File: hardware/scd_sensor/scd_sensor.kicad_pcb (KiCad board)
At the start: 2 copper layers, 18.6 x 27.4 mm, 10 parts, among them J1 Conn_01x03, J5 Conn_02x10_Odd_Even, U1 SCD41-D-R2, U2 TPS76333, U3 SGP40-D-R4

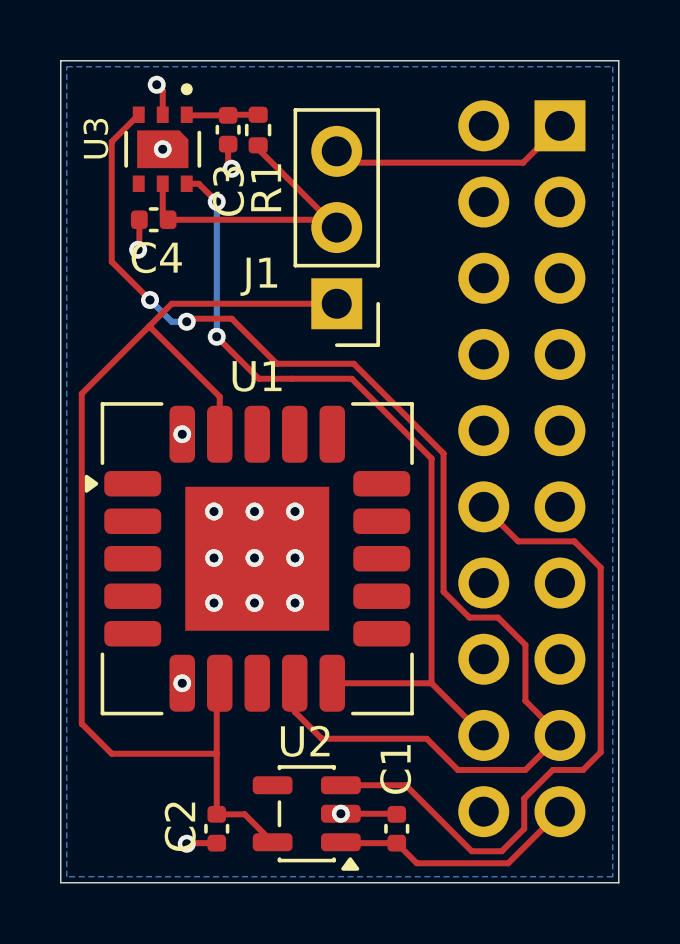
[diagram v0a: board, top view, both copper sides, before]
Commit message: Fix SDA/SCL placement on SGP40
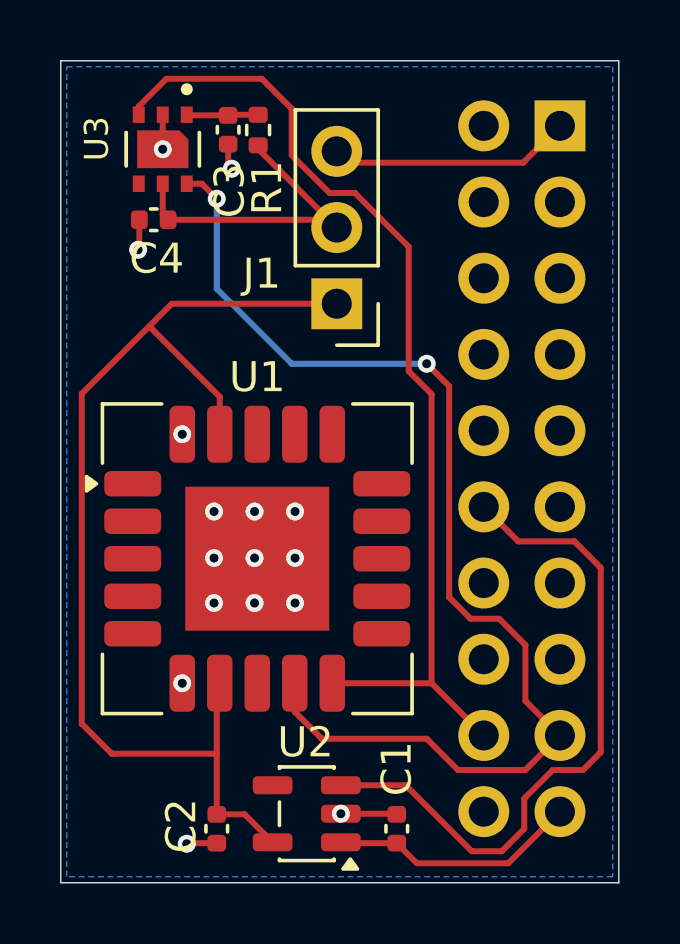
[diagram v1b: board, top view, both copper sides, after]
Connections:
- U3 pad 3: /SCL -> /SDA
- U3 pad 6: /SDA -> /SCL
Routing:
- net /SDA: track 27.9 -> 33.5 mm, vias 2 -> 0
- net /SCL: track 41.7 -> 38.1 mm
- net GND: track 5.85 -> 5.89 mm, vias 17 -> 16
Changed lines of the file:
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@@
 			(size 0.55 0.4)
 			(layers "F.Cu" "F.Mask" "F.Paste")
-			(net 13 "/SCL")
+			(net 9 "/SDA")
 			(pinfunction "SDA")
 			(pintype "bidirectional")
@@
 			(size 0.55 0.4)
 			(layers "F.Cu" "F.Mask" "F.Paste")
-			(net 9 "/SDA")
+			(net 13 "/SCL")
 			(pinfunction "SCL")
 			(pintype "bidirectional")
@@
 	)
 	(segment
-		(start 134 96.5)
-		(end 134.4 96.5)
+		(start 137.5 95.54776)
+		(end 137.5 94)
 		(width 0.2)
 		(layer "F.Cu")
@@
 	)
 	(segment
-		(start 142.16 105.66)
-		(end 142.16 113.15)
+		(start 142.16 103.509943)
+		(end 141.399 102.748943)
 		(width 0.2)
 		(layer "F.Cu")
@@
 	)
 	(segment
-		(start 136.4 103)
-		(end 135 101.6)
+		(start 132.4 93.923)
+		(end 132.4 94.2)
 		(width 0.2)
 		(layer "F.Cu")
@@
 	)
 	(segment
-		(start 137.5 103)
-		(end 136.4 103)
+		(start 136.5 93)
+		(end 133.323 93)
 		(width 0.2)
 		(layer "F.Cu")
@@
 	)
 	(segment
-		(start 137.5 103)
-		(end 139.5 103)
+		(start 141.399 102.748943)
+		(end 141.399 98.601)
 		(width 0.2)
 		(layer "F.Cu")
@@
 	)
 	(segment
-		(start 134.4 96.5)
-		(end 135 97.1)
+		(start 141.399 98.601)
+		(end 139.607 96.809)
 		(width 0.2)
 		(layer "F.Cu")
@@
 	)
 	(segment
-		(start 139.5 103)
-		(end 142.16 105.66)
+		(start 133.323 93)
+		(end 132.4 93.923)
+		(width 0.2)
+		(layer "F.Cu")
+		(net 9)
+	)
+	(segment
+		(start 138.76124 96.809)
+		(end 137.5 95.54776)
+		(width 0.2)
+		(layer "F.Cu")
+		(net 9)
+	)
+	(segment
+		(start 142.16 113.15)
+		(end 142.16 103.509943)
+		(width 0.2)
+		(layer "F.Cu")
+		(net 9)
+	)
+	(segment
+		(start 139.607 96.809)
+		(end 138.76124 96.809)
+		(width 0.2)
+		(layer "F.Cu")
+		(net 9)
+	)
+	(segment
+		(start 137.5 94)
+		(end 136.5 93)
 		(width 0.2)
 		(layer "F.Cu")
@@
 		(net 9)
 	)
-	(via
-		(at 135 101.6)
-		(size 0.6)
-		(drill 0.3)
-		(layers "F.Cu" "B.Cu")
-		(net 9)
-	)
-	(via
-		(at 135 97.1)
-		(size 0.6)
-		(drill 0.3)
-		(layers "F.Cu" "B.Cu")
-		(net 9)
-	)
-	(segment
-		(start 135 101.6)
-		(end 135 97.1)
-		(width 0.2)
-		(layer "B.Cu")
-		(net 9)
-	)
-	(segment
-		(start 146.44 114.89)
-		(end 145.289 113.739)
-		(width 0.2)
-		(layer "F.Cu")
-		(net 13)
-	)
-	(segment
-		(start 137 102.5)
-		(end 135.499 100.999)
-		(width 0.2)
-		(layer "F.Cu")
-		(net 13)
-	)
-	(segment
-		(start 135.499 100.999)
-		(end 134.101 100.999)
-		(width 0.2)
-		(layer "F.Cu")
-		(net 13)
-	)
 	(segment
 		(start 145.289 116.041)
@@
 	)
 	(segment
-		(start 132.775735 100.375735)
-		(end 131.5 99.1)
-		(width 0.2)
-		(layer "F.Cu")
-		(net 13)
-	)
-	(segment
 		(start 137.6 114.1)
 		(end 137.6 113.15)
@@
 	)
 	(segment
-		(start 144.37676 110.961)
-		(end 143.42324 110.961)
+		(start 142.749 110.28676)
+		(end 143.46224 111)
+		(width 0.2)
+		(layer "F.Cu")
+		(net 13)
+	)
+	(segment
+		(start 145.289 111.87324)
+		(end 145.289 113.739)
+		(width 0.2)
+		(layer "F.Cu")
+		(net 13)
+	)
+	(segment
+		(start 142 102.5)
+		(end 142.749 103.249)
 		(width 0.2)
 		(layer "F.Cu")
@@
 	)
 	(segment
+		(start 144.41576 111)
+		(end 145.289 111.87324)
+		(width 0.2)
+		(layer "F.Cu")
+		(net 13)
+	)
+	(segment
 		(start 142 115)
 		(end 138.5 115)
@@
 	)
 	(segment
-		(start 145.289 113.739)
-		(end 145.289 111.87324)
-		(width 0.2)
-		(layer "F.Cu")
-		(net 13)
-	)
-	(segment
-		(start 139.5671 102.5)
-		(end 137 102.5)
-		(width 0.2)
-		(layer "F.Cu")
-		(net 13)
-	)
-	(segment
-		(start 142.561 110.09876)
-		(end 142.561 105.4939)
-		(width 0.2)
-		(layer "F.Cu")
-		(net 13)
-	)
-	(segment
-		(start 145.289 111.87324)
-		(end 144.37676 110.961)
-		(width 0.2)
-		(layer "F.Cu")
-		(net 13)
-	)
-	(segment
-		(start 143.42324 110.961)
-		(end 142.561 110.09876)
+		(start 143.46224 111)
+		(end 144.41576 111)
+		(width 0.2)
+		(layer "F.Cu")
+		(net 13)
+	)
+	(segment
+		(start 142.749 103.249)
+		(end 142.749 110.28676)
 		(width 0.2)
 		(layer "F.Cu")
@@
 	)
 	(segment
-		(start 131.5 99.1)
-		(end 131.5 95.1)
-		(width 0.2)
-		(layer "F.Cu")
-		(net 13)
-	)
-	(segment
-		(start 131.5 95.1)
-		(end 132.4 94.2)
-		(width 0.2)
-		(layer "F.Cu")
-		(net 13)
-	)
-	(segment
-		(start 142.561 105.4939)
-		(end 139.5671 102.5)
-		(width 0.2)
-		(layer "F.Cu")
-		(net 13)
-	)
-	(segment
-		(start 134.101 100.999)
-		(end 134 101.1)
-		(width 0.2)
-		(layer "F.Cu")
-		(net 13)
-	)
-	(via
-		(at 134 101.1)
-		(size 0.6)
-		(drill 0.3)
-		(layers "F.Cu" "B.Cu")
-		(net 13)
-	)
-	(via
-		(at 132.775735 100.375735)
-		(size 0.6)
-		(drill 0.3)
-		(layers "F.Cu" "B.Cu")
-		(net 13)
-	)
-	(segment
-		(start 133.5 101.1)
-		(end 132.775735 100.375735)
+		(start 134.5 96.5)
+		(end 135 97)
+		(width 0.2)
+		(layer "F.Cu")
+		(net 13)
+	)
+	(segment
+		(start 134 96.5)
+		(end 134.5 96.5)
+		(width 0.2)
+		(layer "F.Cu")
+		(net 13)
+	)
+	(segment
+		(start 145.289 113.739)
+		(end 146.44 114.89)
+		(width 0.2)
+		(layer "F.Cu")
+		(net 13)
+	)
+	(via
+		(at 142 102.5)
+		(size 0.6)
+		(drill 0.3)
+		(layers "F.Cu" "B.Cu")
+		(net 13)
+	)
+	(via
+		(at 135 97)
+		(size 0.6)
+		(drill 0.3)
+		(layers "F.Cu" "B.Cu")
+		(net 13)
+	)
+	(segment
+		(start 135 100)
+		(end 137.5 102.5)
 		(width 0.2)
 		(layer "B.Cu")
@@
 	)
 	(segment
-		(start 134 101.1)
-		(end 133.5 101.1)
+		(start 137.5 102.5)
+		(end 142 102.5)
 		(width 0.2)
 		(layer "B.Cu")
@@
 	)
 	(segment
-		(start 133.2 93.4)
-		(end 133 93.2)
-		(width 0.2)
-		(layer "F.Cu")
-		(net 15)
-	)
-	(segment
-		(start 133.2 94.2)
-		(end 133.2 93.4)
-		(width 0.2)
-		(layer "F.Cu")
-		(net 15)
+		(start 135 97)
+		(end 135 100)
+		(width 0.2)
+		(layer "B.Cu")
+		(net 13)
 	)
 	(segment
@@
 	)
 	(segment
+		(start 133.2 94.2)
+		(end 133.2 95.35)
+		(width 0.2)
+		(layer "F.Cu")
+		(net 15)
+	)
+	(segment
 		(start 135.38 95.18)
 		(end 135.38 95.88)
@@
 		(net 15)
 	)
-	(segment
-		(start 140.98 117.5)
-		(end 141 117.52)
-		(width 0.2)
-		(layer "F.Cu")
-		(net 15)
-	)
 	(via
 		(at 133.85 113.15)
@@
 	(via
 		(at 139.1375 117.5)
-		(size 0.6)
-		(drill 0.3)
-		(layers "F.Cu" "B.Cu")
-		(net 15)
-	)
-	(via
-		(at 133 93.2)
 		(size 0.6)
 		(drill 0.3)
@@
 		(width 0.2)
 		(layer "F.Cu")
-		(net 20)
-	)
-	(segment
-		(start 135 113.25)
-		(end 135.1 113.15)
-		(width 0.2)
-		(layer "F.Cu")

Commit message: Add pin names to the board
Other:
- board text added: "3V3|GND"
- board text added: "SCL|SDA"
- board text added: "SYS"
- board text added: "x|PWR_EN"
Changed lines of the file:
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@@
 			(sketchdnponfab yes)
 			(crossoutdnponfab yes)
-			(subtractmaskfromsilk no)
+			(subtractmaskfromsilk yes)
 			(outputformat 1)
 			(mirror no)
@@
 		(tags "Through hole pin header THT 2x10 2.54mm double row")
 		(property "Reference" "J5"
-			(at 5.44 0.77 0)
+			(at 1.245175 -11.43 0)
 			(layer "B.SilkS")
 			(effects
@@
 		(layer "Edge.Cuts")
 	)
+	(gr_text "SYS"
+		(at 142 118 0)
+		(layer "B.SilkS")
+		(effects
+			(font
+				(size 1 1)
+				(thickness 0.1)
+			)
+			(justify left bottom mirror)
+		)
+	)
+	(gr_text "x|PWR_EN"
+		(at 142 107.5 0)
+		(layer "B.SilkS")
+		(effects
+			(font
+				(size 1 1)
+				(thickness 0.1)
+			)
+			(justify left bottom mirror)
+		)
+	)
 	(gr_text "CO2 Sensor\n"
 		(at 132 99.5 90)
@@
 	)
 	(gr_text "SCD4x"
-		(at 138 111.5 90)
+		(at 134 110.5 90)
 		(layer "B.SilkS")
 		(effects
@@
 		)
 	)
+	(gr_text "3V3|GND"
+		(at 142 94 0)
+		(layer "B.SilkS")
+		(effects
+			(font
+				(size 1 1)
+				(thickness 0.1)
+			)
+			(justify left bottom mirror)
+		)
+	)
 	(gr_text "SGP40"
-		(at 138 93 90)
+		(at 134 95.5 90)
 		(layer "B.SilkS")
 		(effects
@@
 			)
 			(justify left bottom mirror)
+		)
+	)
+	(gr_text "SCL|SDA"
+		(at 142 115.5 0)
+		(layer "B.SilkS")
+		(effects
+			(font
+				(size 1 1)
+				(thickness 0.1)
+			)
+			(justify left bottom mirror)
